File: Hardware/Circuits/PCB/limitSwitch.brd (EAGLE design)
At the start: 84 x 66.3 mm, 9 parts

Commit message: circuits
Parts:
- removed POWER_LED_M, POWER_LED_M1: LEDFAB1206, fab:LED1206FAB
- added J1, J2: (no value), SparkFun-Connectors:1X06_NO_SILK
- added JP1, JP2, JP3: JUMPER-SMT_2_NC_TRACE_NO-SILK, SparkFun-Jumpers:SMT-JUMPER_2_NC_TRACE_NO-SILK
- added LED_STOP, POWER_LED: LEDFAB1206, fab:LED1206FAB
- added M_02, M_03: (no value), SparkFun-Connectors:1X06-1MM
- moved POWER_LED_RES1 47.9 mm to (6.60, 17.5)
- moved POWER_LED_RES 36.8 mm to (11.7, 17.5)
- moved R2 24.5 mm to (11.7, 22.6)
- moved R1 24.5 mm to (6.60, 22.6)
- moved M_01 14.5 mm to (35.6, 7.62), flipped to the bottom, turned to 270 degrees
- moved SWITCH_M2 0.57 mm to (52.6, 48.0)
- moved SWITCH_M1 0.25 mm to (12.7, 48.0)
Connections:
- removed net LED_IN: M_01.4, POWER_LED_RES.2
- removed net NEO_PIXEL: M_01.3
- new net LED_IN_1: JP1.1, M_01.4, POWER_LED_RES.2
- new net LED_IN_2: JP3.1, M_01.3, POWER_LED_RES1.2
- new net N$2: JP2.1, R2.2, SWITCH_M2.2
- new net SWITCH_03: J1.4, J2.4, M_02.4, M_03.4
- new net SWITCH_04: J1.3, J2.3, M_02.3, M_03.3
- net GND_MCU: now also J1.1, J2.1, LED_STOP.2, M_02.1, M_03.1, POWER_LED.2; no longer POWER_LED_M.2, POWER_LED_M1.2
- net N$1: now also POWER_LED.1; no longer POWER_LED_M1.1
- net N$11: now also LED_STOP.1; no longer POWER_LED_M.1
- net SWITCH_01: now also J1.6, J2.6, JP1.2, M_02.6, M_03.6
- net SWITCH_02: now also J1.5, J2.5, JP2.2, JP3.2, M_02.5, M_03.5; no longer R2.2, SWITCH_M2.2
- net VCC_MCU: now also J1.2, J2.2, M_02.2, M_03.2; no longer POWER_LED_RES1.2
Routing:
- net N$2: track 0.00 -> 77.0 mm, vias 0 -> 1
- net SWITCH_01: track 56.3 -> 118.0 mm, vias 0 -> 4
- net LED_IN_1: track 0.00 -> 58.0 mm, vias 0 -> 2
- net LED_IN_2: track 0.00 -> 44.6 mm, vias 0 -> 2
- net SWITCH_04: track 0.00 -> 33.8 mm
- net SWITCH_03: track 0.00 -> 32.5 mm, vias 0 -> 1
- net N$1: track 42.7 -> 75.2 mm, vias 0 -> 1
- net VCC_MCU: track 73.8 -> 106.1 mm
- net SWITCH_02: track 46.6 -> 60.2 mm, vias 0 -> 1
- net LED_IN: track 8.86 -> 0.00 mm
- net N$11: track 52.6 -> 49.8 mm, vias 2 -> 1
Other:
- board text added: "-"
- board text added: "10K"
- board text added: "500"
- board text added: "GND"
- board text added: "Power 01"
- board text added: "Power 02"
- board text added: "switch 02"

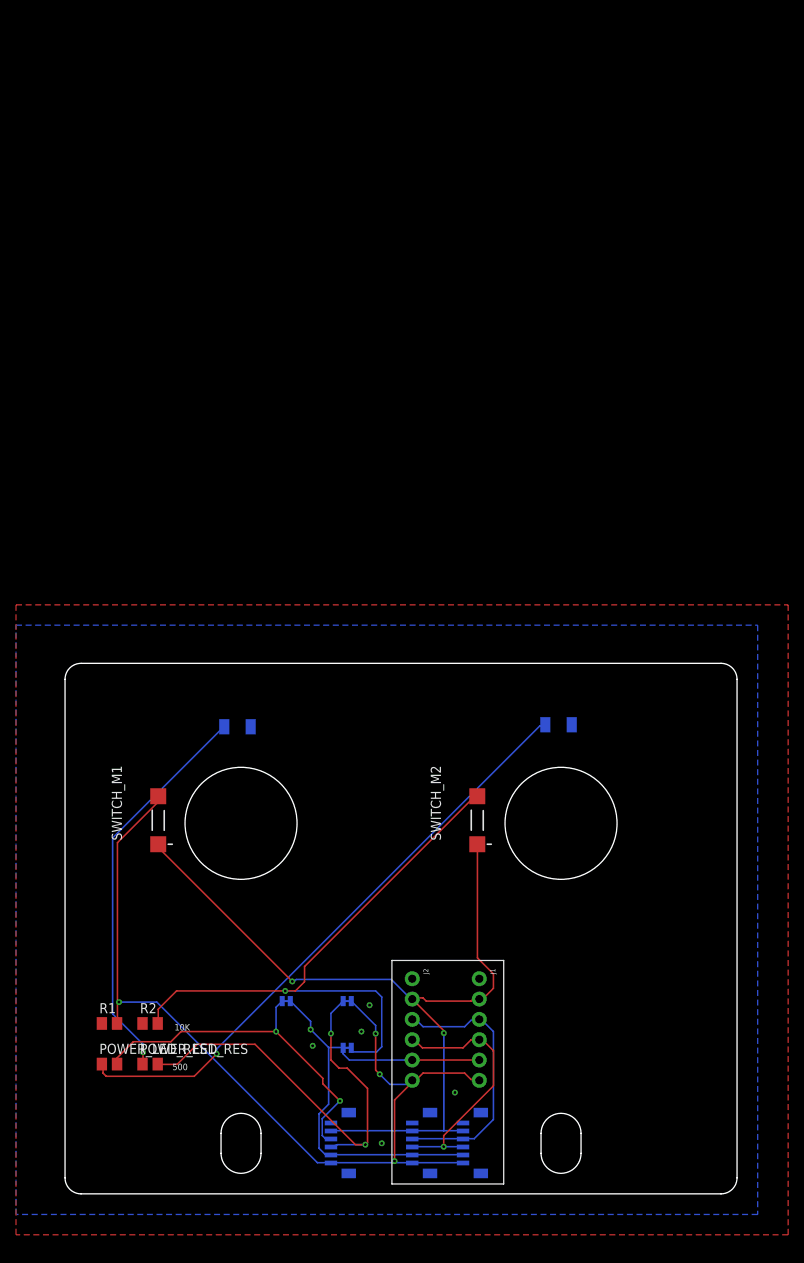
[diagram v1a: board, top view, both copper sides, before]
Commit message: enable Motor
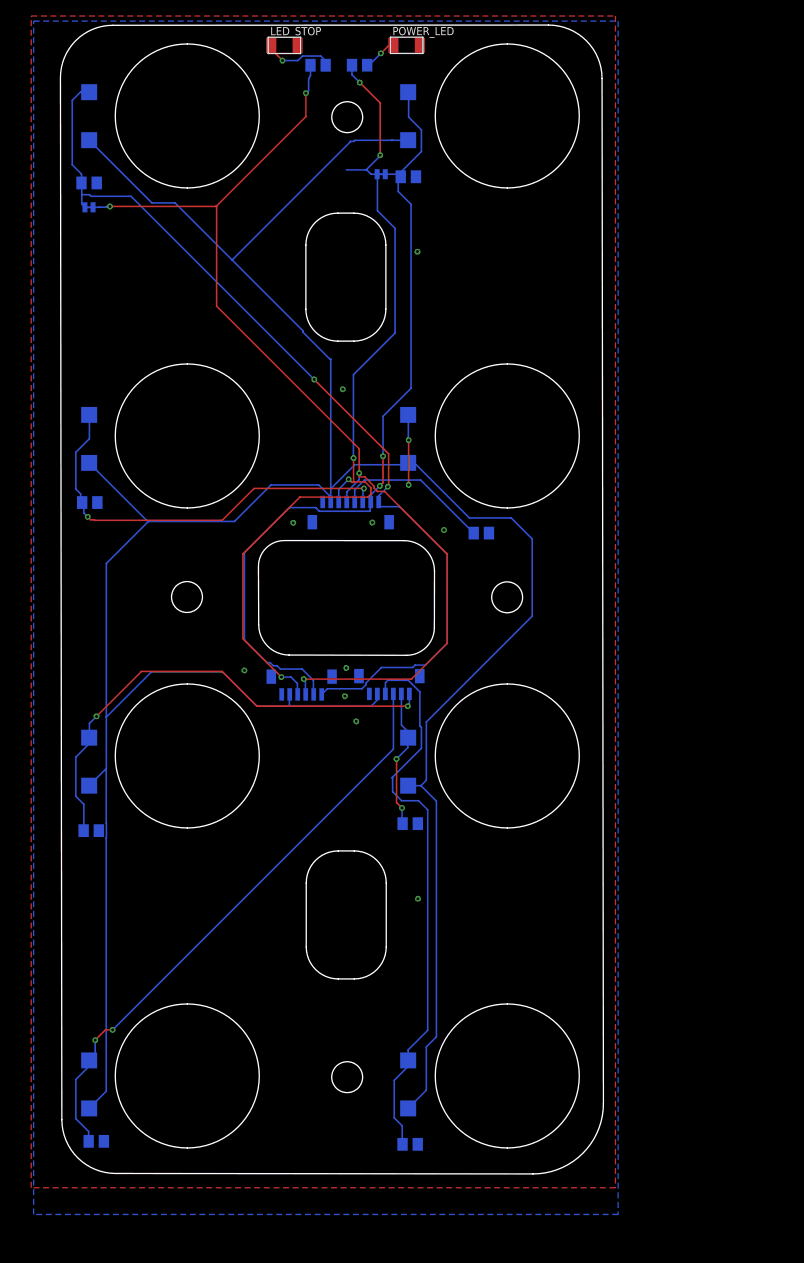
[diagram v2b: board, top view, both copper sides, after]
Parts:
- removed J1, J2: (no value), SparkFun-Connectors:1X06_NO_SILK
- removed JP2: JUMPER-SMT_2_NC_TRACE_NO-SILK, SparkFun-Jumpers:SMT-JUMPER_2_NC_TRACE_NO-SILK
- removed M_02: (no value), SparkFun-Connectors:1X06-1MM
- added J3: (no value), SparkFun-Connectors:BM08B-SRSS-TB
- added R3, R4, R5, R6, R7, R8: 10k, resistor:M0805
- added SWITCH_M3, SWITCH_M4, SWITCH_M5, SWITCH_M6, SWITCH_M7, SWITCH_M8: DTSM-3, switch-tact:DTSM-3
- moved POWER_LED_RES1 128.7 mm to (37.9, 142.4), flipped to the bottom
- moved POWER_LED_RES 126.6 mm to (32.7, 142.4), flipped to the bottom
- moved R2 110.6 mm to (44.0, 128.4), flipped to the bottom
- moved R1 105.1 mm to (4.06, 127.7), flipped to the bottom
- moved JP1 104.3 mm to (4.05, 124.6), turned to 0 degrees
- moved JP3 104.0 mm to (40.6, 128.8)
- moved SWITCH_M1 88.4 mm to (4.06, 136.0), flipped to the bottom
- moved SWITCH_M2 88.4 mm to (43.9, 136.0), flipped to the bottom
- moved POWER_LED 87.0 mm to (43.7, 144.9), flipped to the top, turned to 0 degrees
- moved LED_STOP 85.4 mm to (28.5, 144.9), flipped to the top, turned to 0 degrees
- moved M_03 57.6 mm to (41.6, 65.1), turned to 180 degrees
- moved M_01 57.6 mm to (30.7, 65.0), turned to 180 degrees
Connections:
- removed net N$2: JP2.1, R2.2, SWITCH_M2.2
- new net SWITCH_05: M_03.6, R5.2, SWITCH_M5.2
- new net SWITCH_06: M_03.5, R6.2, SWITCH_M6.2
- new net SWITCH_07: M_03.4, R7.2, SWITCH_M7.2
- new net SWITCH_08: M_03.3, R8.2, SWITCH_M8.2
- net GND_MCU: now also J3.1, R3.1, R4.1, R5.1, R6.1, R7.1, R8.1; no longer J1.1, J2.1, M_02.1
- net LED_IN_1: now also J3.4
- net LED_IN_2: now also J3.3
- net SWITCH_01: now also J3.8; no longer J1.6, J2.6, M_02.6, M_03.6
- net SWITCH_02: now also J3.7, R2.2, SWITCH_M2.2; no longer J1.5, J2.5, JP2.2, M_02.5, M_03.5
- net SWITCH_03: now also J3.6, R3.2, SWITCH_M3.2; no longer J1.4, J2.4, M_02.4, M_03.4
- net SWITCH_04: now also J3.5, R4.2, SWITCH_M4.2; no longer J1.3, J2.3, M_02.3, M_03.3
- net VCC_MCU: now also J3.2, SWITCH_M3.1, SWITCH_M4.1, SWITCH_M5.1, SWITCH_M6.1, SWITCH_M7.1, SWITCH_M8.1; no longer J1.2, J2.2, M_02.2
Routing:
- net VCC_MCU: track 106.1 -> 355.0 mm, vias 2 -> 0
- net N$2: track 77.0 -> 0.00 mm, vias 1 -> 0
- net LED_IN_1: track 58.0 -> 131.6 mm, vias 2 -> 4
- net SWITCH_07: track 0.00 -> 73.6 mm, vias 0 -> 2
- net N$1: track 75.2 -> 4.35 mm
- net SWITCH_08: track 0.00 -> 70.8 mm
- net LED_IN_2: track 44.6 -> 108.9 mm, vias 2 -> 5
- net SWITCH_05: track 0.00 -> 60.4 mm, vias 0 -> 2
- net SWITCH_02: track 60.2 -> 101.3 mm, vias 1 -> 2
- net N$11: track 49.8 -> 8.90 mm
- net SWITCH_03: track 32.5 -> 52.2 mm, vias 1 -> 2
- net SWITCH_06: track 0.00 -> 17.5 mm, vias 0 -> 2
- net SWITCH_04: track 33.8 -> 29.1 mm, vias 0 -> 2
- net SWITCH_01: track 118.0 -> 115.9 mm, vias 4 -> 2
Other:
- board size 84 x 66.3 mm -> 67.9 x 143.6 mm
- board text removed: "10K"
- board text removed: "500"
- board text removed: "GND"
- board text removed: "Power 01"
- board text removed: "Power 02"
- board text removed: "switch 02"

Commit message: update circuits
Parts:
- removed J3: (no value), SparkFun-Connectors:BM08B-SRSS-TB
- added M_02: (no value), SparkFun-Connectors:1X06-1MM
- moved JP1 30.9 mm to (32.9, 135.6), turned to 180 degrees
- moved M_01 19.0 mm to (36.3, 83.1)
- moved JP3 7.82 mm to (37.4, 135.9)
- moved POWER_LED 7.03 mm to (38.0, 140.9), flipped to the bottom
- moved LED_STOP 5.89 mm to (32.8, 140.8), flipped to the bottom
- moved M_03 4.76 mm to (42.0, 60.3)
- moved POWER_LED_RES1 4.04 mm to (37.9, 138.3)
- moved POWER_LED_RES 4.04 mm to (32.7, 138.3)
- moved R1 4.04 mm to (4.06, 123.6)
- moved R3 4.04 mm to (4.14, 83.7)
- moved R4 4.04 mm to (53.1, 79.9)
- moved SWITCH_M3 4.04 mm to (4.06, 91.6)
- moved SWITCH_M4 4.04 mm to (43.9, 91.6)
- moved SWITCH_M5 4.04 mm to (4.06, 51.3)
- moved SWITCH_M6 4.04 mm to (43.9, 51.3)
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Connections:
- net GND_MCU: now also M_02.1; no longer J3.1
- net LED_IN_1: no longer J3.4
- net LED_IN_2: no longer J3.3
- net SWITCH_01: now also M_02.3; no longer J3.8
- net SWITCH_02: now also M_02.4; no longer J3.7
- net SWITCH_03: now also M_02.5; no longer J3.6
- net SWITCH_04: now also M_02.6; no longer J3.5
- net VCC_MCU: now also M_02.2; no longer J3.2
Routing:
- net LED_IN_1: track 131.6 -> 65.2 mm, vias 4 -> 2
- net VCC_MCU: track 355.0 -> 309.8 mm, vias 0 -> 8
- net SWITCH_01: track 115.9 -> 157.6 mm, vias 2 -> 4
- net LED_IN_2: track 108.9 -> 68.1 mm, vias 5 -> 2
- net SWITCH_04: track 29.1 -> 51.0 mm
- net SWITCH_08: track 70.8 -> 58.3 mm, vias 0 -> 2
- net N$11: track 8.90 -> 2.90 mm, vias 1 -> 0
- net SWITCH_02: track 101.3 -> 105.0 mm, vias 2 -> 3
- net SWITCH_03: track 52.2 -> 55.6 mm
- net N$1: track 4.35 -> 2.86 mm, vias 1 -> 0
- net SWITCH_07: track 73.6 -> 72.5 mm
- net SWITCH_05: track 60.4 -> 59.4 mm, vias 2 -> 0
- net SWITCH_06: track 17.5 -> 17.4 mm, vias 2 -> 0

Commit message: update circuits
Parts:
- added J1: (no value), SparkFun-Connectors:1X01
- added R9: 10k, resistor:M0805
- moved R4 9.99 mm to (44.0, 83.9)
- moved POWER_LED_RES 0.46 mm to (32.7, 137.9)
- moved JP3 0.42 mm to (37.8, 135.7)
- moved POWER_LED_RES1 0.36 mm to (37.9, 138.0)
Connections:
- net GND_MCU: now also R9.1
- net VCC_MCU: now also J1.1, R9.2
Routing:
- net GND_MCU: track 0.00 -> 29.0 mm, vias 0 -> 6
- net VCC_MCU: track 309.8 -> 320.9 mm
- net LED_IN_1: track 65.2 -> 69.8 mm
- net SWITCH_04: track 51.0 -> 55.0 mm
- net SWITCH_02: track 105.0 -> 107.1 mm
- net SWITCH_01: track 157.6 -> 159.0 mm
- net SWITCH_05: track 59.4 -> 60.5 mm
- net LED_IN_2: track 68.1 -> 69.2 mm
- net SWITCH_03: track 55.6 -> 56.3 mm
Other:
- outline, holes or cut-outs redrawn
- board text added: "LIMIT - 01-02 LED"
- board text added: "LIMIT 01-04"
- board text added: "LIMIT 05-08"

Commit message: comments
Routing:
- net SWITCH_01: track 159.0 -> 159.5 mm
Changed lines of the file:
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@@
 <wire x1="32.2873" y1="60.83798125" x2="32.2873" y2="58.934584375" width="0.2" layer="16"/>
 <wire x1="32.2873" y1="60.83798125" x2="31.318340625" y2="60.83798125" width="0.2" layer="1"/>
-<wire x1="31.318340625" y1="60.83798125" x2="31.290121875" y2="60.8097625" width="0.2" layer="1"/>
-<wire x1="29.6491" y1="60.8097625" x2="31.290121875" y2="60.8097625" width="0.2" layer="1"/>
-<wire x1="24" y1="66.4588625" x2="29.6491" y2="60.8097625" width="0.2" layer="1"/>
+<wire x1="31.318340625" y1="60.83798125" x2="31.3180625" y2="60.837703125" width="0.2" layer="1"/>
+<wire x1="29.621159375" y1="60.837703125" x2="31.3180625" y2="60.837703125" width="0.2" layer="1"/>
+<wire x1="24" y1="66.4588625" x2="29.621159375" y2="60.837703125" width="0.2" layer="1"/>
 <wire x1="24" y1="77.4588625" x2="24" y2="66.4588625" width="0.2" layer="1"/>
 <wire x1="29.1" y1="82.5588625" x2="24" y2="77.4588625" width="0.2" layer="1"/>
@@
 <via x="27.50311875" y="58.83148125" extent="1-16" drill="0.35"/>
 <via x="38.935659375" y="56.949340625" extent="1-16" drill="0.35"/>
-<wire x1="27.50311875" y1="58.83148125" x2="34.2268375" y2="58.83148125" width="0.4" layer="1"/>
-<wire x1="34.2268375" y1="58.83148125" x2="34.87765625" y2="58.1806625" width="0.4" layer="1"/>
-<wire x1="37.7043375" y1="58.1806625" x2="38.935659375" y2="56.949340625" width="0.4" layer="1"/>
-<wire x1="34.87765625" y1="58.1806625" x2="37.7043375" y2="58.1806625" width="0.4" layer="1"/>
+<wire x1="27.50311875" y1="58.83148125" x2="28.08731875" y2="58.24728125" width="0.4" layer="1"/>
+<wire x1="31.130578125" y1="58.24728125" x2="28.08731875" y2="58.24728125" width="0.4" layer="1"/>
+<wire x1="31.130578125" y1="58.24728125" x2="32.713575" y2="56.664284375" width="0.4" layer="1"/>
+<wire x1="38.935659375" y1="56.949340625" x2="38.650603125" y2="56.664284375" width="0.4" layer="1"/>
+<wire x1="38.650603125" y1="56.664284375" x2="32.713575" y2="56.664284375" width="0.4" layer="1"/>
 <wire x1="38.935659375" y1="56.949340625" x2="38.935659375" y2="58.5571625" width="0.4" layer="16"/>
 <wire x1="38.935659375" y1="58.5571625" x2="39.430959375" y2="59.0524625" width="0.4" layer="16"/>
@@
 <wire x1="33.1495375" y1="133.54558125" x2="31.244540625" y2="133.54558125" width="0.2" layer="16"/>
 <wire x1="31.2593625" y1="61.6367625" x2="31.2593625" y2="58.881175" width="0.2" layer="16"/>
-<wire x1="32.6779" y1="61.6367625" x2="31.2593625" y2="61.6367625" width="0.2" layer="1"/>
-<wire x1="34.4" y1="63.3588625" x2="32.6779" y2="61.6367625" width="0.2" layer="1"/>
-<wire x1="45.6" y1="63.3588625" x2="34.4" y2="63.3588625" width="0.2" layer="1"/>
+<wire x1="31.2593625" y1="61.6367625" x2="31.2593625" y2="62.610903125" width="0.2" layer="1"/>
+<wire x1="32.007321875" y1="63.3588625" x2="31.2593625" y2="62.610903125" width="0.2" layer="1"/>
+<wire x1="45.6" y1="63.3588625" x2="32.007321875" y2="63.3588625" width="0.2" layer="1"/>
 <wire x1="48.4" y1="66.1588625" x2="45.6" y2="63.3588625" width="0.2" layer="1"/>
 <wire x1="48.4" y1="77.1588625" x2="48.4" y2="66.1588625" width="0.2" layer="1"/>
